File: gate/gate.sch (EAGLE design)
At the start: 25 parts, among them J1 MOLEX_MINILITE_TRAP_2, J2 MOLEX_MINILITE_TRAP_2, J3 MOLEX_MINILITE_TRAP_2, J4 MOLEX_MINILITE_TRAP_2, J5 MOLEX_MINILITE_TRAP_2, J6 MOLEX_MINILITE_TRAP_2, J7 MOLEX_MINILITE_TRAP_2, J8 MOLEX_MINILITE_TRAP_2, J9 MOLEX_MINILITE_TRAP_2, U1 SN75468

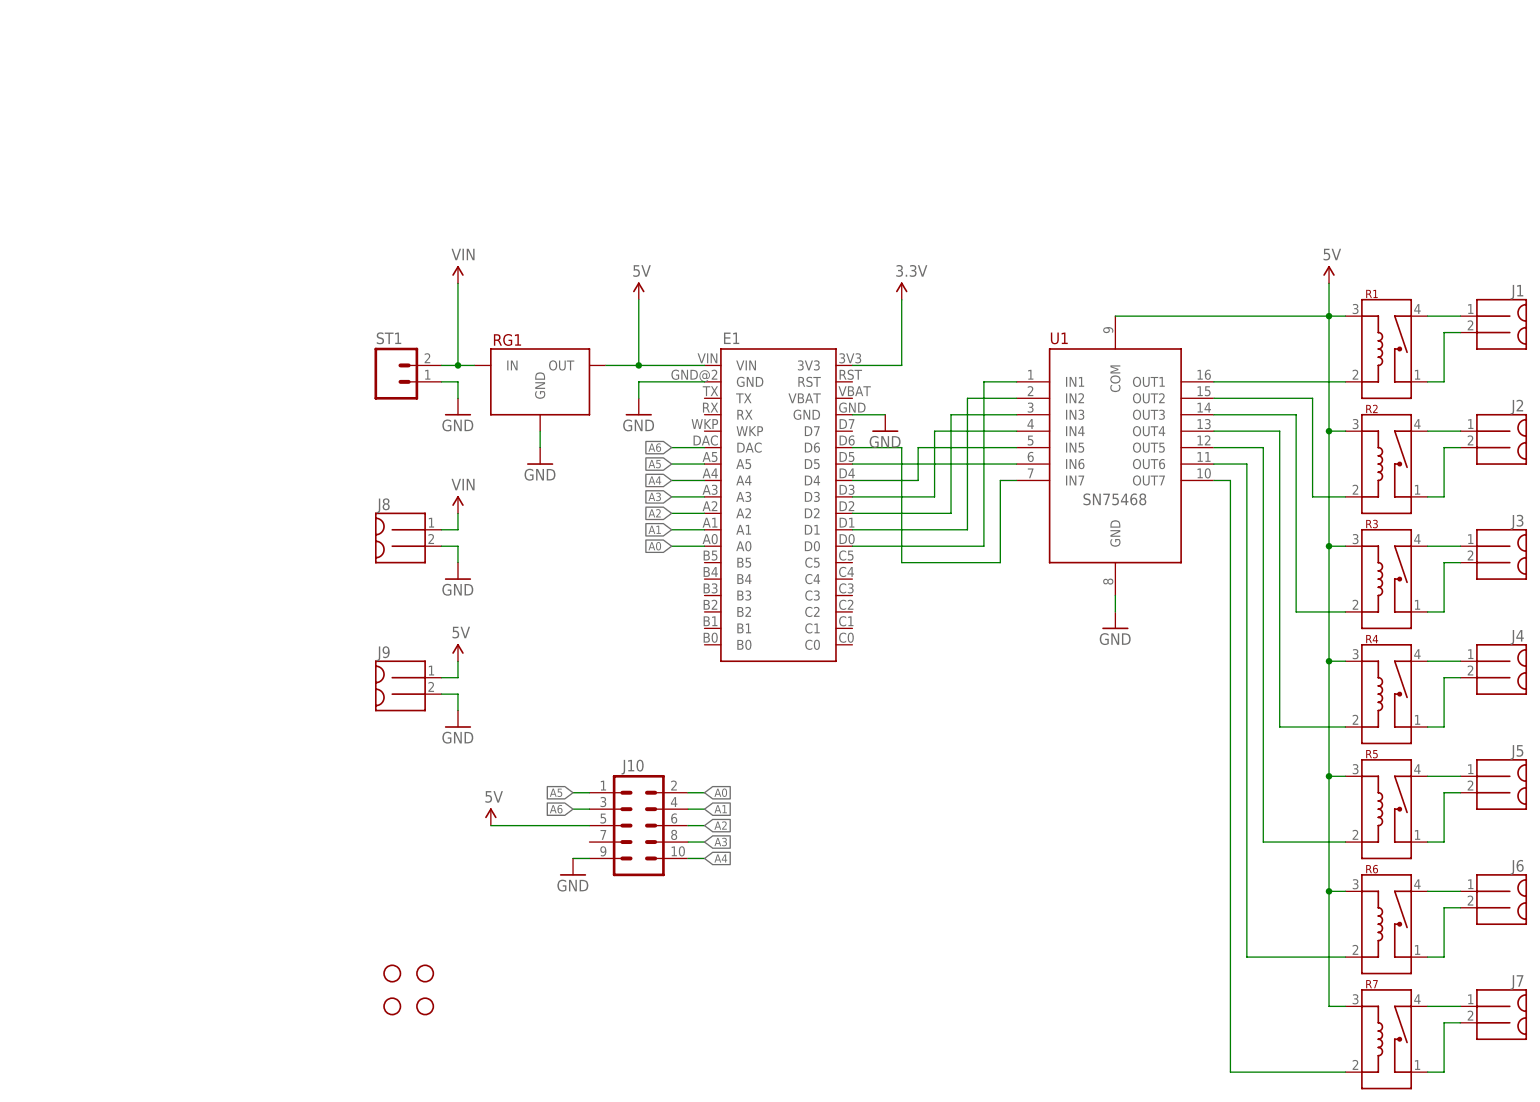
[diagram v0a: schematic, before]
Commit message: Clean up old files, move gate6 to gate
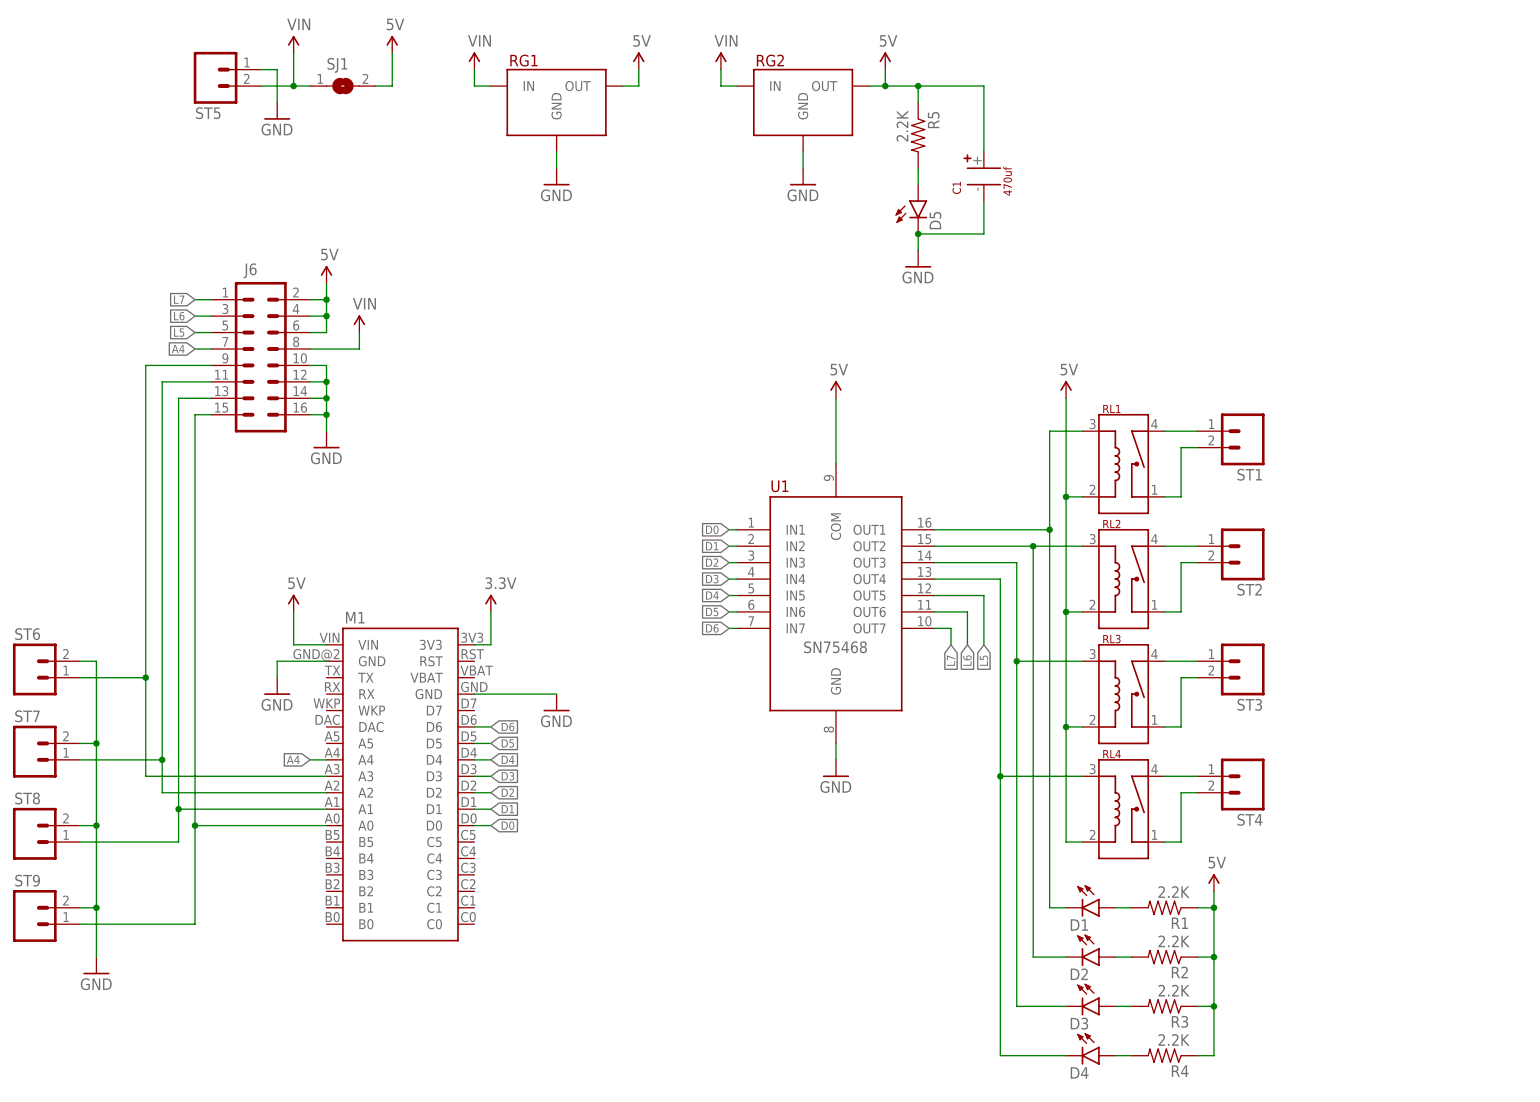
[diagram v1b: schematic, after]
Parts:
- removed E1: ELECTRON, Puffin:ELECTRON
- removed H1, H2, H3, H4: STAND-OFF, SparkFun-Electromechanical:STAND-OFF
- removed J1, J2, J3, J4, J5, J7, J8, J9: MOLEX_MINILITE_TRAP_2, Puffin:MOLEX_MINILITE_TRAP_2
- removed J10: (no value), SparkFun-Connectors:M05X2PTH
- removed R6, R7: HE3600_RELAY, Puffin:HE3600_RELAY
- added C1: 470uf, Puffin:CAPACITOR-AXIAL10X25
- added D1, D2, D3, D4, D5: (no value), SparkFun-LED:LED0603
- added M1: ELECTRON, Puffin:ELECTRON
- added RG2: TRACO_TSR_2, Puffin:TRACO_TSR_2
- added RL1, RL2, RL3, RL4: HE3600_RELAY, Puffin:HE3600_RELAY
- added SJ1: (no value), jumper:SJ
- added ST2, ST3, ST4, ST5, ST6, ST7, ST8, ST9: (no value), Puffin:SCREWTERM_2
- J6: value MOLEX_MINILITE_TRAP_2 -> (none); device Puffin:MOLEX_MINILITE_TRAP_2 -> SparkFun-Connectors:M08X2
- R1, R2, R3, R4, R5: value HE3600_RELAY -> 2.2K; device Puffin:HE3600_RELAY -> SparkFun-Resistors:RESISTOR0603
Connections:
- removed net A0: E1.A0, J10.2
- removed net A1: E1.A1, J10.4
- removed net A2: E1.A2, J10.6
- removed net A3: E1.A3, J10.8
- removed net A5: E1.A5, J10.1
- removed net A6: E1.DAC, J10.3
- removed net N$34: R6.R1, U1.OUT6
- removed net N$36: J5.1, R5.C2
- removed net N$37: J5.2, R5.C1
- removed net N$38: J6.1, R6.C2
- removed net N$39: J6.2, R6.C1
- removed net N$40: J7.1, R7.C2
- removed net N$41: J7.2, R7.C1
- removed net N$42: E1.D4, U1.IN5
- removed net N$43: E1.D5, U1.IN6
- removed net N$44: E1.D6, U1.IN7
- new net D0: M1.D0, U1.IN1
- new net D1: M1.D1, U1.IN2
- new net D2: M1.D2, U1.IN3
- new net D3: M1.D3, U1.IN4
- new net D4: M1.D4, U1.IN5
- new net D5: M1.D5, U1.IN6
- new net D6: M1.D6, U1.IN7
- new net L5: J6.5, U1.OUT5
- new net L6: J6.3, U1.OUT6
- new net L7: J6.1, U1.OUT7
- new net N$1: D2.A, R2.2
- new net N$18: J6.9, M1.A3, ST6.1
- new net N$22: D2.C, RL2.R2, U1.OUT2
- net 3.3V: now also M1.3V3; no longer E1.3V3
- net 5V: now also C1.+, J6.2, J6.4, J6.6, M1.VIN, R1.1, R2.1, R3.1, R4.1, R5.1, RG2.OUT, RL1.R1, RL2.R1, RL3.R1, RL4.R1, SJ1.2; no longer E1.VIN, J10.5, J9.1, R1.R2, R2.R2, R3.R2, R4.R2, R5.R2, R6.R2, R7.R2
- net A4: now also J6.7, M1.A4; no longer E1.A4, J10.10
- net GND: now also C1.-, D5.C, J6.10, J6.12, J6.14, J6.16, M1.GND, M1.GND@2, RG2.GND, ST5.1, ST6.2, ST7.2, ST8.2, ST9.2; no longer E1.GND, E1.GND@2, J10.9, J8.2, J9.2, ST1.1
- net N$10: now also RL3.C1, ST3.2; no longer J3.1, R3.C2
- net N$11: now also RL4.C1, ST4.2; no longer J3.2, R3.C1
- net N$12: now also RL1.C2, ST1.1; no longer J4.1, R4.C2
- net N$13: now also RL1.C1, ST1.2; no longer J4.2, R4.C1
- net N$14: now also D5.A, R5.2; no longer E1.D0, U1.IN1
- net N$15: now also J6.15, M1.A0, ST9.1; no longer E1.D1, U1.IN2
- net N$16: now also J6.13, M1.A1, ST8.1; no longer E1.D2, U1.IN3
- net N$17: now also J6.11, M1.A2, ST7.1; no longer E1.D3, U1.IN4
- net N$2: now also D4.C, RL4.R2, U1.OUT4; no longer R1.R1, U1.OUT1
- net N$3: now also D1.A, R1.2; no longer R2.R1, U1.OUT2
- net N$33: now also D1.C, RL1.R2, U1.OUT1; no longer R5.R1, U1.OUT5
- net N$35: now also D3.C, RL3.R2, U1.OUT3; no longer R7.R1, U1.OUT7
- net N$4: now also D3.A, R3.2; no longer R3.R1, U1.OUT3
- net N$5: now also D4.A, R4.2; no longer R4.R1, U1.OUT4
- net N$6: now also RL4.C2, ST4.1; no longer J1.1, R1.C2
- net N$7: now also RL3.C2, ST3.1; no longer J1.2, R1.C1
- net N$8: now also RL2.C2, ST2.1; no longer J2.1, R2.C2
- net N$9: now also RL2.C1, ST2.2; no longer J2.2, R2.C1
- net VIN: now also J6.8, RG2.IN, SJ1.1, ST5.2; no longer J8.1, ST1.2
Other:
- moved on the sheet: RG1, ST1, U1

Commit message: Gate to 2 relays and enclosure fit
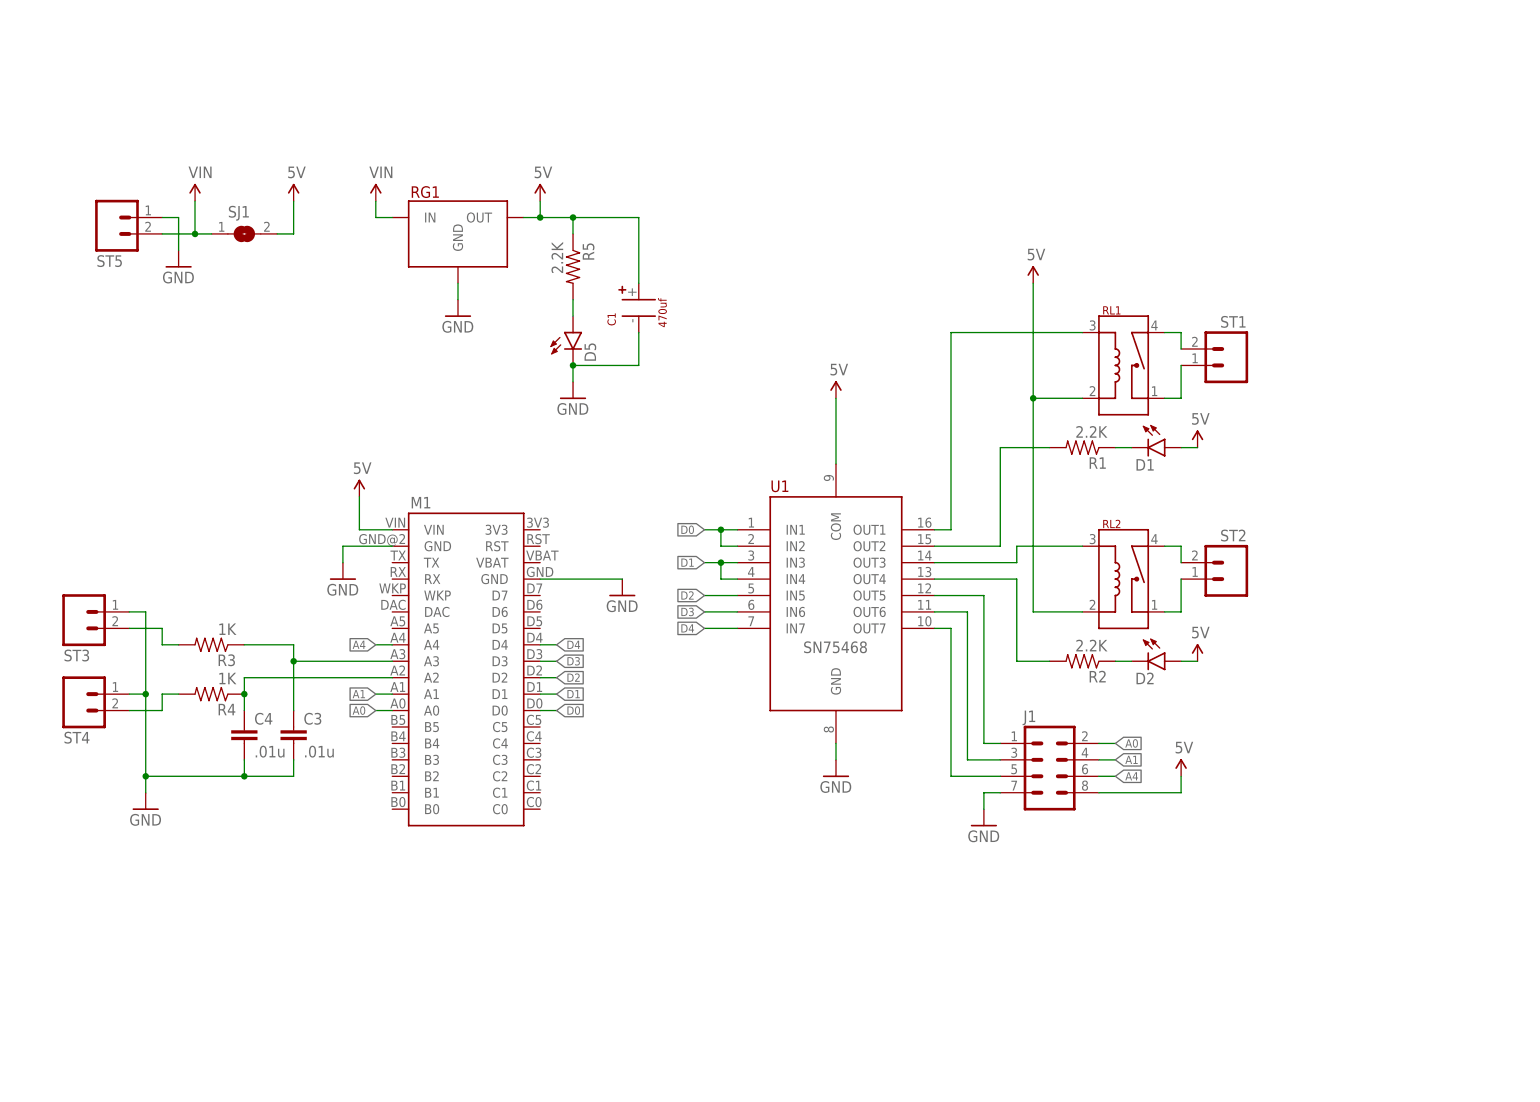
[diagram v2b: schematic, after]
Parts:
- removed D3, D4: (no value), SparkFun-LED:LED0603
- removed J6: (no value), SparkFun-Connectors:M08X2
- removed RG2: TRACO_TSR_2, Puffin:TRACO_TSR_2
- removed RL3, RL4: HE3600_RELAY, Puffin:HE3600_RELAY
- removed ST6, ST7, ST8, ST9: (no value), Puffin:SCREWTERM_2
- added C3, C4: .01u, SparkFun-Capacitors:CAP0603-CAP
- added J1: (no value), SparkFun-Connectors:M04X2
- R3, R4: value 2.2K -> 1K
- RG1: value (none) -> TRACO_TSR_2; device Puffin:MURATA_REG -> Puffin:TRACO_TSR_2
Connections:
- removed net 3.3V: M1.3V3
- removed net D5: M1.D5, U1.IN6
- removed net D6: M1.D6, U1.IN7
- removed net N$10: RL3.C1, ST3.2
- removed net N$11: RL4.C1, ST4.2
- removed net N$12: RL1.C2, ST1.1
- removed net N$15: J6.15, M1.A0, ST9.1
- removed net N$16: J6.13, M1.A1, ST8.1
- removed net N$35: D3.C, RL3.R2, U1.OUT3
- new net A0: J1.2, M1.A0
- new net A1: J1.4, M1.A1
- net 5V: now also D1.A, D2.A, J1.8; no longer J6.2, J6.4, J6.6, R1.1, R2.1, R3.1, R4.1, RG2.OUT, RL3.R1, RL4.R1
- net A4: now also J1.6; no longer J6.7
- net D0: now also U1.IN2
- net D1: now also U1.IN3, U1.IN4; no longer U1.IN2
- net D2: now also U1.IN5; no longer U1.IN3
- net D3: now also U1.IN6; no longer U1.IN4
- net D4: now also U1.IN7; no longer U1.IN5
- net GND: now also C3.2, C4.2, J1.7, ST3.1, ST4.1; no longer J6.10, J6.12, J6.14, J6.16, RG2.GND, ST6.2, ST7.2, ST8.2, ST9.2
- net L5: now also J1.1; no longer J6.5
- net L6: now also J1.3; no longer J6.3
- net L7: now also J1.5; no longer J6.1
- net N$1: now also D2.C, R2.1; no longer D2.A, R2.2
- net N$13: now also ST1.1; no longer ST1.2
- net N$17: now also R4.2, ST4.2; no longer J6.11, M1.A2, ST7.1
- net N$18: now also R3.2, ST3.2; no longer J6.9, M1.A3, ST6.1
- net N$2: now also RL1.C2, ST1.2; no longer D4.C, RL4.R2, U1.OUT4
- net N$22: now also U1.OUT3; no longer D2.C, U1.OUT2
- net N$3: now also D1.C, R1.1; no longer D1.A, R1.2
- net N$33: no longer D1.C
- net N$4: now also RL2.C2, ST2.2; no longer D3.A, R3.2
- net N$5: now also R2.2, U1.OUT4; no longer D4.A, R4.2
- net N$6: now also R1.2, U1.OUT2; no longer RL4.C2, ST4.1
- net N$7: now also C4.1, M1.A2, R4.1; no longer RL3.C2, ST3.1
- net N$8: now also C3.1, M1.A3, R3.1; no longer RL2.C2, ST2.1
- net N$9: now also ST2.1; no longer ST2.2
- net VIN: no longer J6.8, RG2.IN
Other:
- moved on the sheet: C1, D1, D2, D5, M1, R1, R2, R3, R4, R5, RL1, SJ1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

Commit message: Gate: Fix ext header, move pwr led. misc cleanup.
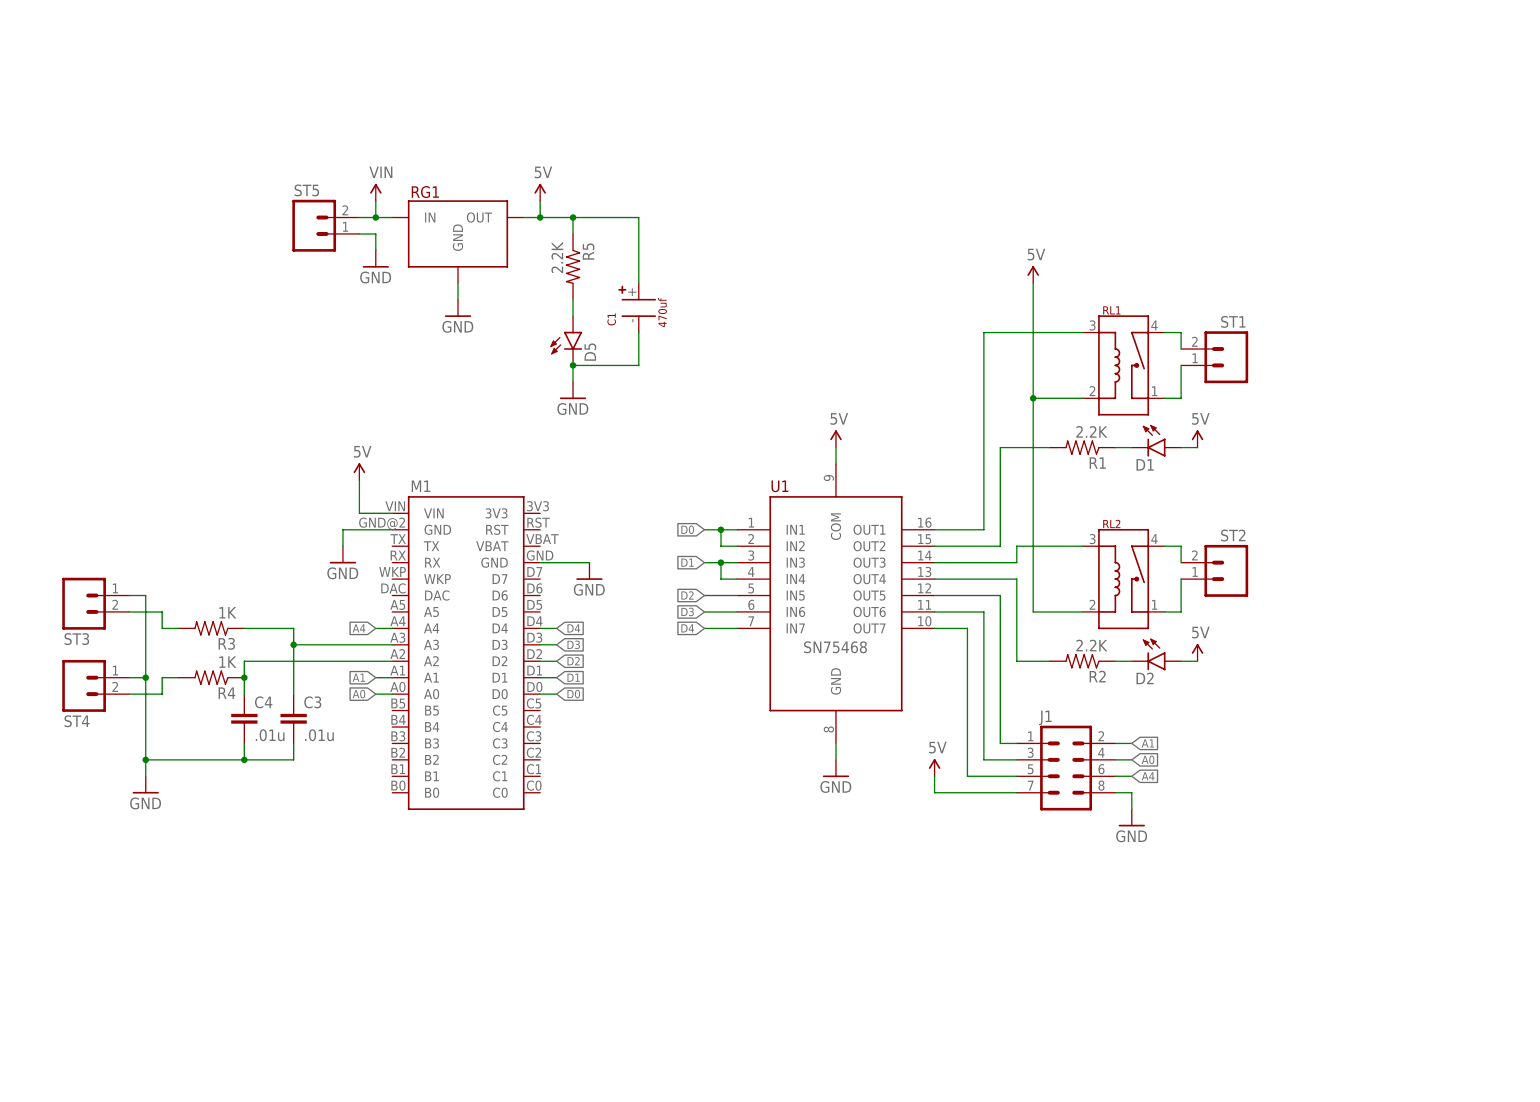
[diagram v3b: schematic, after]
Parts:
- removed SJ1: (no value), jumper:SJ
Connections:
- net 5V: now also J1.7; no longer J1.8, SJ1.2
- net A0: now also J1.4; no longer J1.2
- net A1: now also J1.2; no longer J1.4
- net GND: now also J1.8; no longer J1.7
- net VIN: no longer SJ1.1
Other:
- moved on the sheet: C3, C4, J1, M1, R3, R4, ST3, ST4, ST5
